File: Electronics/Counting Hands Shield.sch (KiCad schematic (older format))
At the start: 29 parts, among them P1 Arduino P0-P7, P10 Servo_3, P11 Servo_4, P12 Servo_5, P2 Arduino P8-SCL, P3 Arduino A5-A0, P4 Arduino Vin-Blank, P5 LEDs Anodes, P6 LEDs Cat, P7 Servo_H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

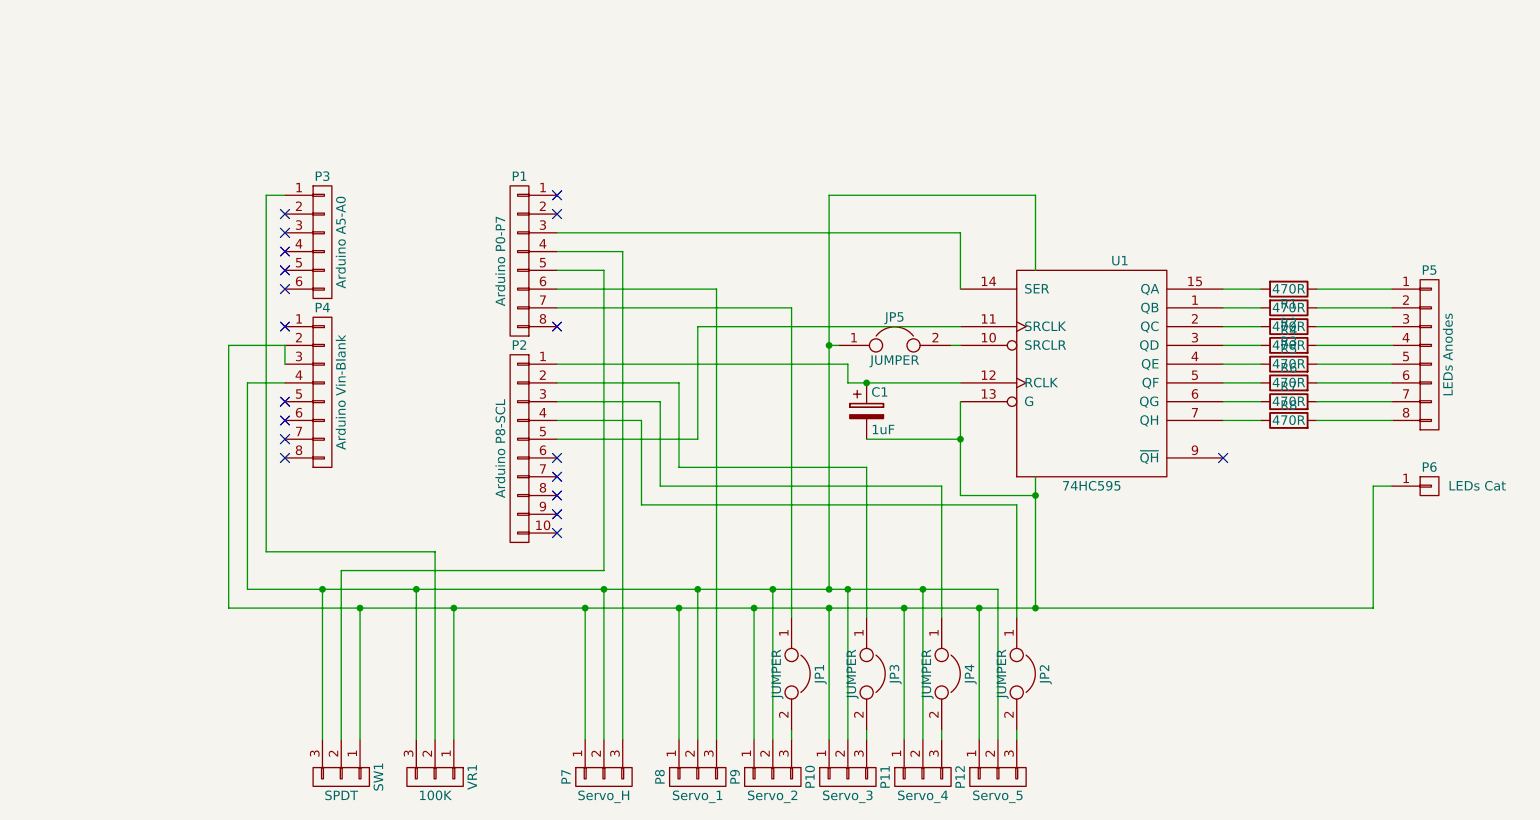
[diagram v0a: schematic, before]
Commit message: Changes to KiCAD project
Replaced Potentiometer (VR1) with Rotary Encoder (P6)

Added 2DIP switch for default interval

Replaced 8 LEDs progress indicator and 74HC595 Shift Register with 4 digit 7 Segment Display
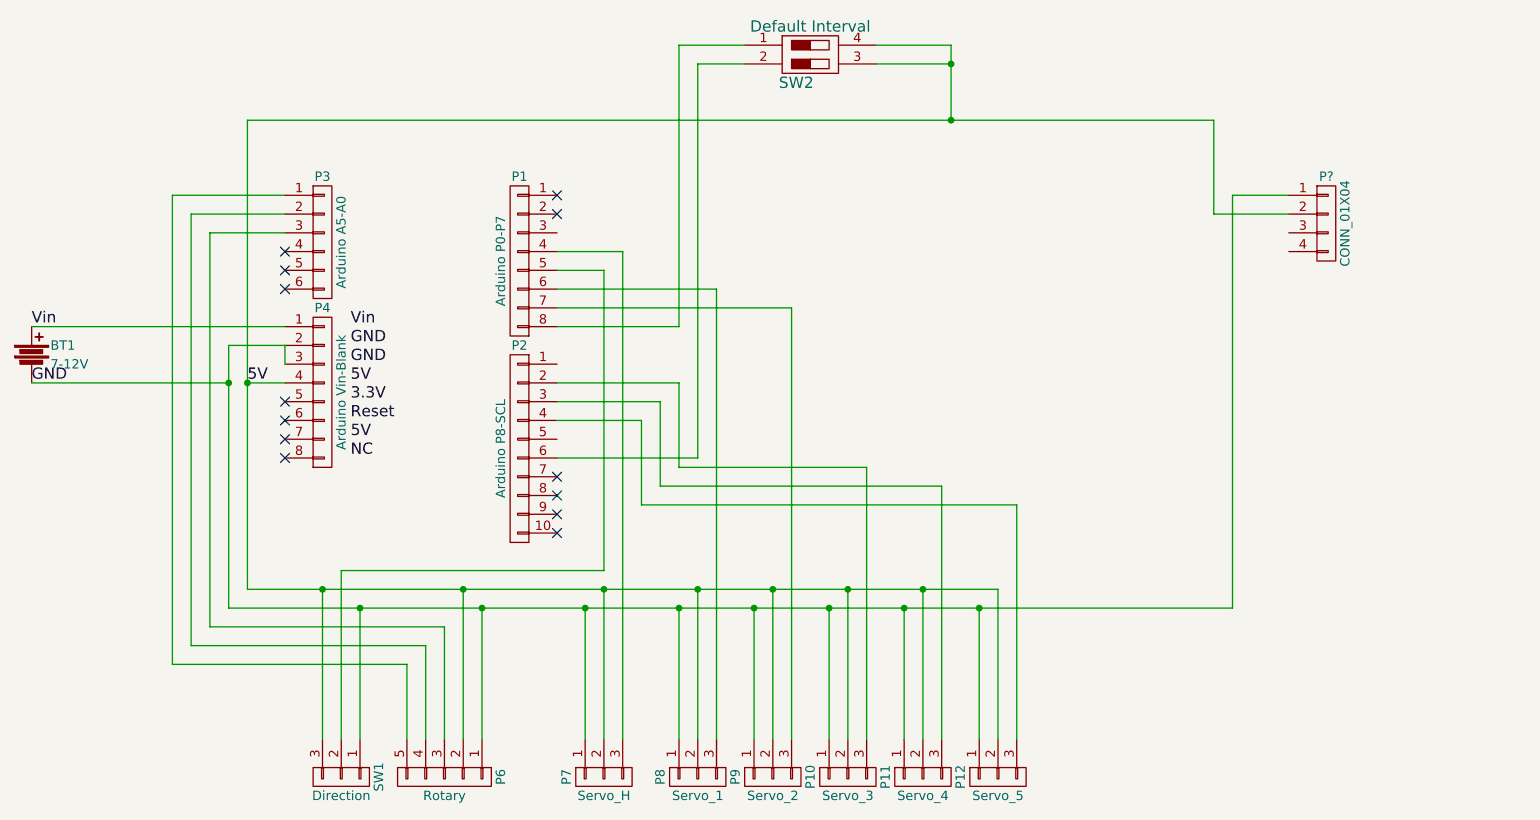
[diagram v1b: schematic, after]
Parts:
- removed C1: 1uF, Capacitors_ThroughHole:C_Radial_D5_L11_P2, symbol CP
- removed JP1, JP2, JP3, JP4, JP5: JUMPER, Personal:Jumper, symbol JUMPER
- removed P5: LEDs Anodes, Pin_Headers:Pin_Header_Straight_1x08, symbol CONN_01X08
- removed P6: LEDs Cat, Pin_Headers:Pin_Header_Straight_1x01, symbol CONN_01X01
- removed R1, R2, R3, R4, R5, R6, R7, R8: 470R, Resistors_ThroughHole:Resistor_Horizontal_RM10mm, symbol R
- removed U1: 74HC595, Housings_DIP:DIP-16_W7.62mm_LongPads, symbol 74HC595
- removed VR1: 100K, Pin_Headers:Pin_Header_Straight_1x03, symbol CONN_01X03
- added BT1: 7-12V, Terminal_Blocks:TerminalBlock_Pheonix_MKDS1.5-2pol, symbol Battery
- added P6: Rotary, Pin_Headers:Pin_Header_Straight_1x05, symbol CONN_01X05
- added P?: CONN_01X04, symbol CONN_01X04
- added SW2: Default Interval, Buttons_Switches_ThroughHole:SW_DIP_x2_Slide, symbol DIP_Switch_2
- SW1: value SPDT -> Direction
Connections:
- net GND: now also BT1.2, P6.1 (P1), P?.1 (P1)
- net at P1.7 (P7): now also P9.3 (P3)
- net at P1.8 (P8): now also SW2.1
- net at P2.2 (P2): now also P10.3 (P3)
- net at P2.3 (P3): now also P11.3 (P3)
- net at P2.4 (P4): now also P12.3 (P3)
- net at P2.6 (P6): now also SW2.2
- net at P3.1 (P1): now also P6.5 (P5)
- net at P3.2 (P2): now also P6.4 (P4)
- net at P3.3 (P3): now also P6.3 (P3)
- net Vin: now reaches P4.1 (P1)
- net Vin: now also BT1.1
- net VCC renamed 5V
- net 5V: now also P6.2 (P2), P?.2 (P2), SW2.3, SW2.4
- no-connect marks 19 -> 13

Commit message: Changes to KiCAD project
Tidied up schematic and PCB
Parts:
- P5: renamed from P?; value CONN_01X04 -> 4x7 Segment Display; footprint (none) -> Pin_Headers:Pin_Header_Straight_1x04
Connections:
- net at P1.8 (P8): now also SW2.2; no longer SW2.1
- net at P2.1 (P1): now also SW2.1
- net at P2.6 (P6): no longer SW2.2
- net at P3.4 (P4): now also P5.3 (P3)
- net at P3.5 (P5): now also P5.4 (P4)
- no-connect marks 13 -> 12
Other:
- moved on the sheet: P5, SW2
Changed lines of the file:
@@
 	0    1    1    0
 $EndComp
-NoConn ~ 3050 2600
-NoConn ~ 3050 2700
 NoConn ~ 3050 2800
 NoConn ~ 4500 2300
@@
 L DIP_Switch_2 SW2
 U 1 1 57E00F78
-P 5850 1550
-F 0 "SW2" H 5775 1400 60  0000 C CNN
-F 1 "Default Interval" H 5850 1700 60  0000 C CNN
-F 2 "Buttons_Switches_ThroughHole:SW_DIP_x2_Slide" H 5850 1400 60  0001 C CNN
-F 3 "" H 5850 1400 60  0001 C CNN
-	1    5850 1550
-	1    0    0    -1
+P 3750 1650
+F 0 "SW2" H 3675 1500 60  0000 C CNN
+F 1 "Default Interval" H 3750 1800 60  0000 C CNN
+F 2 "Buttons_Switches_ThroughHole:SW_DIP_x2_Slide" H 3750 1500 60  0001 C CNN
+F 3 "" H 3750 1500 60  0001 C CNN
+	1    3750 1650
+	-1   0    0    -1
 $EndComp
 Connection ~ 5150 4500
@@
 Connection ~ 5950 4500
 Connection ~ 6350 4500
-Connection ~ 6750 4500
 Connection ~ 5250 4400
 Connection ~ 5650 4400
@@
 Connection ~ 3450 4500
 Wire Wire Line
-	2850 1900 2850 4400
+	2850 1600 2850 4400
 Connection ~ 3250 4400
 Wire Wire Line
@@
 Wire Wire Line
 	6550 3850 6550 5200
-Wire Wire Line
-	8000 1900 2850 1900
 Connection ~ 2850 3300
-Connection ~ 6600 1900
 Wire Wire Line
 	4100 5200 4100 4500
@@
 	3700 4800 3700 5200
 Wire Wire Line
-	4500 3700 5250 3700
-Wire Wire Line
-	5250 3700 5250 1600
-Wire Wire Line
-	5250 1600 5500 1600
-Wire Wire Line
-	5500 1500 5150 1500
-Wire Wire Line
-	5150 1500 5150 3000
-Wire Wire Line
 	5150 3000 4500 3000
-Wire Wire Line
-	6200 1600 6600 1600
-Wire Wire Line
-	6200 1500 6600 1500
-Connection ~ 6600 1600
 Wire Wire Line
 	6150 3750 6150 5200
@@
 Text Label 2850 3300 0    60   ~ 0
 5V
-Wire Wire Line
-	6600 1500 6600 1900
-Wire Wire Line
-	2750 4500 8100 4500
-$Comp
-L CONN_01X04 P?
+$Comp
+L CONN_01X04 P5
 U 1 1 57EFA040
-P 8600 2450
-F 0 "P?" H 8600 2700 50  0000 C CNN
-F 1 "CONN_01X04" V 8700 2450 50  0000 C CNN
-F 2 "" H 8600 2450 50  0000 C CNN
-F 3 "" H 8600 2450 50  0000 C CNN
-	1    8600 2450
-	1    0    0    -1
-$EndComp
-Wire Wire Line
-	8000 2400 8400 2400
-Wire Wire Line
-	8000 1900 8000 2400
-Wire Wire Line
-	8400 2300 8100 2300
-Wire Wire Line
-	8100 2300 8100 4500
+P 1800 2550
+F 0 "P5" H 1800 2800 50  0000 C CNN
+F 1 "4x7 Segment Display" V 1900 2550 50  0000 C CNN
+F 2 "Pin_Headers:Pin_Header_Straight_1x04" H 1800 2550 50  0001 C CNN
+F 3 "" H 1800 2550 50  0000 C CNN
+	1    1800 2550
+	-1   0    0    -1
+$EndComp
+Wire Wire Line
+	4500 3200 5250 3200
+Wire Wire Line
+	5250 3200 5250 1600
+NoConn ~ 4500 3700
+Wire Wire Line
+	3050 2600 2000 2600
+Wire Wire Line
+	3050 2700 2000 2700
+Wire Wire Line
+	2350 2500 2000 2500
+Wire Wire Line
+	2000 2400 2250 2400
+Wire Wire Line
+	2250 2400 2250 3300
+Connection ~ 2250 3300
+Wire Wire Line
+	6750 4500 2750 4500
+Wire Wire Line
+	4100 1700 5150 1700
+Wire Wire Line
+	5150 1700 5150 3000
+Wire Wire Line
+	5250 1600 4100 1600
+Wire Wire Line
+	3400 1600 2850 1600
+Connection ~ 2850 1700
+Wire Wire Line
+	2350 2500 2350 2200
+Wire Wire Line
+	2350 2200 2850 2200
+Connection ~ 2850 2200
+Wire Wire Line
+	2850 1700 3400 1700
 $EndSCHEMATC
